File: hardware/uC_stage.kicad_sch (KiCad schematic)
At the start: 0 parts

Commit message: Updates to structure of the schematic. Minor funcitonality adjustments.
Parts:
- added C1, C2 (x4): 1u, Capacitor_SMD:C_0805_2012Metric_Pad1.18x1.45mm_HandSolder, symbol Device:C_Small
- added C2 (x4): 0.1u, Capacitor_SMD:C_0805_2012Metric_Pad1.18x1.45mm_HandSolder, symbol Device:C_Small
- added C2: 10u, Capacitor_SMD:C_0805_2012Metric_Pad1.18x1.45mm_HandSolder, symbol Device:C_Small
- added H1, H2, H3, H4: ~, MountingHole:MountingHole_3.2mm_M3_Pad_Via, symbol Mechanical:MountingHole_Pad
- added R41, R42: ?, Resistor_SMD:R_0805_2012Metric_Pad1.20x1.40mm_HandSolder, symbol Device:R_Small
- added R43, R44, R45: 10k, Resistor_SMD:R_0805_2012Metric_Pad1.20x1.40mm_HandSolder, symbol Device:R_Small
- added U10: STM32F042F6Px, Package_SO:TSSOP-20_4.4x6.5mm_P0.65mm, symbol MCU_ST_STM32F0:STM32F042F6Px
- added U2: MIC5504-1.2YM5, Package_TO_SOT_SMD:SOT-23-5_HandSoldering, symbol Regulator_Linear:MIC5504-1.2YM5
- added U8: MCP4728, Package_SO:MSOP-10_3x3mm_P0.5mm, symbol Analog_DAC:MCP4728
- added U9: DPO2036, User_USB_Protection:UQFN2020-12, symbol User_USB_Protection:DPO2036
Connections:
- new net: C2.1, U9.5 (CB)
- new net: R43.1, U8.6 (VOUTA)
- new net: R44.2, U8.7 (VOUTB)
- new net 3V3_SUPPLY_L: C2.1, C2.1, C2.1, C2.1, C2.1, C2.1, R41.1, R42.1, R45.1, U10.16 (VDD), U10.5 (VDDA), U2.5 (VOUT), U8.1 (VDD), U9.12 (VSYS)
- new net 5V0_SUPPLY_G: C1.1, U2.1 (VIN), U2.3 (EN)
- new net GND: C1.2, C2.2, C2.2, C2.2, C2.2, C2.2, C2.2, C2.2, C2.2, C2.2, H1.1, H2.1, H3.1, H4.1, U10.15 (VSSA), U2.2 (GND), U8.10 (VSS), U9.11 (GND)
- new net USB_C_CC1_G: U9.3 (CC1C)
- new net USB_C_CC2_G: U9.4 (CC2C)
- new net USB_C_DNEG_G: U9.1 (SBU1C)
- new net USB_C_DPOS_G: U9.2 (SBU2C)
- new net USB_C_ISOLATED_DNEG: U9.10 (SBUS1S)
- new net USB_C_ISOLATED_DPOS: U9.9 (SBUS2S)
- new net dacNLDAC_dig_l: U8.4 (~{LDAC})
- new net dacOutA_ang_g: C2.1, R43.2
- new net dacOutB_ang_g: C2.1, R44.1
- new net dacRDY_dig_l: U8.5 (RDY/~{BSY})
- new net ucSCL_com_l: R42.2, U8.2 (SCL)
- new net ucSDA_com_l: R41.2, U8.3 (SDA)
- new net usbCIsolatorFaultc_dig_l: R45.2, U9.6 (FAULTB)
- no-connect marks 0 -> 4
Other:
- note added: "TODO: Check the footprint and symbol pins!"

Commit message: Began initial routing. Schematic still not fully complete.
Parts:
- removed H1, H2, H3, H4: ~, MountingHole:MountingHole_3.2mm_M3_Pad_Via, symbol Mechanical:MountingHole_Pad
- added SW500: RotaryEncoder_Switch, Rotary_Encoder:RotaryEncoder_Alps_EC11E-Switch_Vertical_H20mm, symbol Device:RotaryEncoder_Switch
- renumbered R41 to R400, R42 to R401, R43 to R402, R44 to R403, R45 to R404, U8 to U401, U9 to U402, U10 to U403
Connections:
- net 3V3_SUPPLY_L: no longer C2.1, C2.1, C2.1, C2.1, C2.1, R400.1, R401.1, R404.1, U2.5 (VOUT), U401.1 (VDD), U403.16 (VDD), U403.5 (VDDA)
- net ucSCL_com_l renamed UCSCL_COM_G
- net ucSDA_com_l renamed UCSDA_COM_G
- new net 3V3_SUPPLY_G: C2.1, C2.1, C2.1, C2.1, C2.1, R400.1, R401.1, R404.1, U2.5 (VOUT), U401.1 (VDD), U403.16 (VDD), U403.5 (VDDA)

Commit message: Routing close to completion. Pending review.
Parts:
- removed R400, R401: ?, Resistor_SMD:R_0805_2012Metric_Pad1.20x1.40mm_HandSolder, symbol Device:R_Small
- added R508, R509: 0R, Resistor_SMD:R_0805_2012Metric_Pad1.20x1.40mm_HandSolder, symbol Device:R_Small
- added R510, R511: ?, Resistor_SMD:R_0805_2012Metric_Pad1.20x1.40mm_HandSolder, symbol Device:R_Small
- added TP500 (x9): ~, TestPoint:TestPoint_Pad_D1.0mm, symbol Connector:TestPoint
- added TP519: 3V3, TestPoint:TestPoint_Pad_D1.0mm, symbol Connector:TestPoint
- added TP520: SWDIO, TestPoint:TestPoint_Pad_D1.0mm, symbol Connector:TestPoint
- added TP521: SWDCLK, TestPoint:TestPoint_Pad_D1.0mm, symbol Connector:TestPoint
- added TP522: GND, TestPoint:TestPoint_Pad_D1.0mm, symbol Connector:TestPoint
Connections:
- net 3V3_SUPPLY_L is gone; now on net 3V3_SUPPLY_G: C2.1, U402.12 (VSYS)
- net 3V3_SUPPLY_G: now also R510.1, R511.1, TP500.1, TP519.1
- net GND: now also SW500.C, SW500.S2, TP522.1
- net UCSCL_COM_G: now also U403.1 (PB8), R510.2
- net UCSDA_COM_G: now also U403.2 (PF0), R511.2
- net USB_C_DNEG_G: now also R508.1
- net USB_C_DPOS_G: now also R509.2
- net USB_C_ISOLATED_DNEG: now also U403.17 (PA9/PA11), R508.2
- net USB_C_ISOLATED_DPOS: now also U403.18 (PA10/PA12), R509.1
- net dacNLDAC_dig_l: now also U403.10 (PA4), TP500.1
- net dacOutA_ang_g: now also TP500.1
- net dacOutB_ang_g: now also TP500.1
- net dacRDY_dig_l: now also U403.9 (PA3), TP500.1
- net usbCIsolatorFaultc_dig_l: now also TP500.1
- net encoderA_dig_l: now reaches SW500.A
- net encoderA_dig_l: now also U403.6 (PA0), TP500.1
- net encoderB_dig_l: now reaches SW500.B
- net encoderB_dig_l: now also U403.7 (PA1), TP500.1
- net encoderSW_dig_l: now reaches SW500.S1
- net encoderSW_dig_l: now also U403.8 (PA2), TP500.1
- net opStage2A_ang_g: now reaches U403.11 (PA5)
- net opStage2B_ang_g: now reaches U403.12 (PA6)
- net swdio_com_l: now reaches U403.19 (PA13)
- net swdio_com_l: now also TP520.1
- net swdclk_com_l: now reaches U403.20 (PA14)
- net swdclk_com_l: now also TP521.1
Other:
- moved on the sheet: SW500

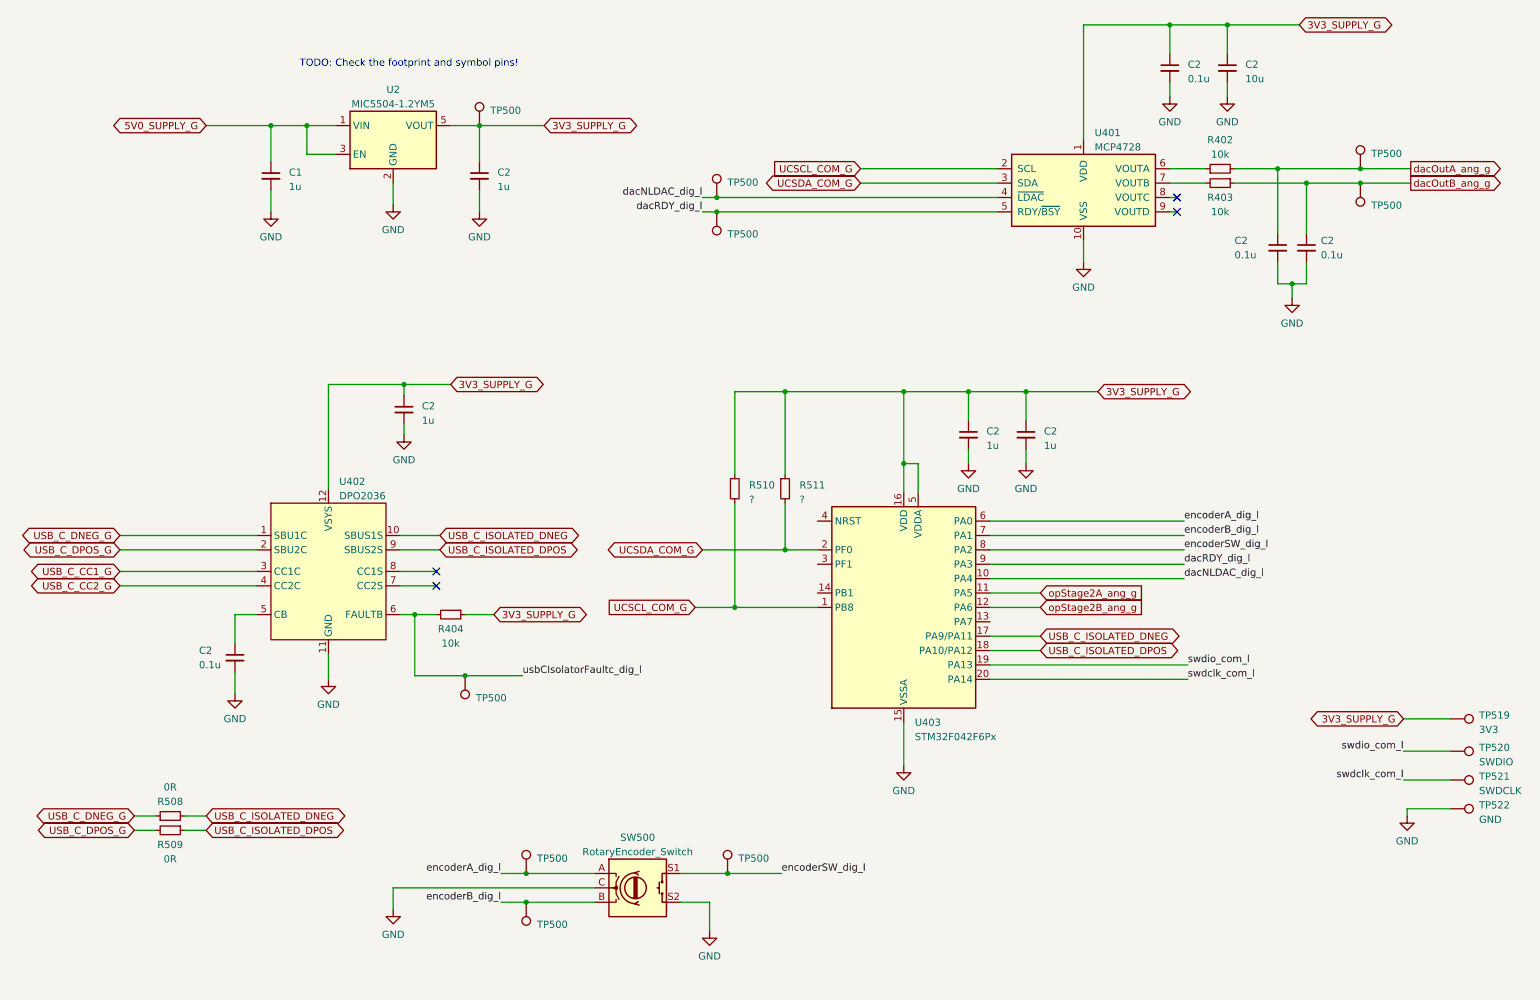
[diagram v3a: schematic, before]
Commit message: Added some doucmentation to MCP driver
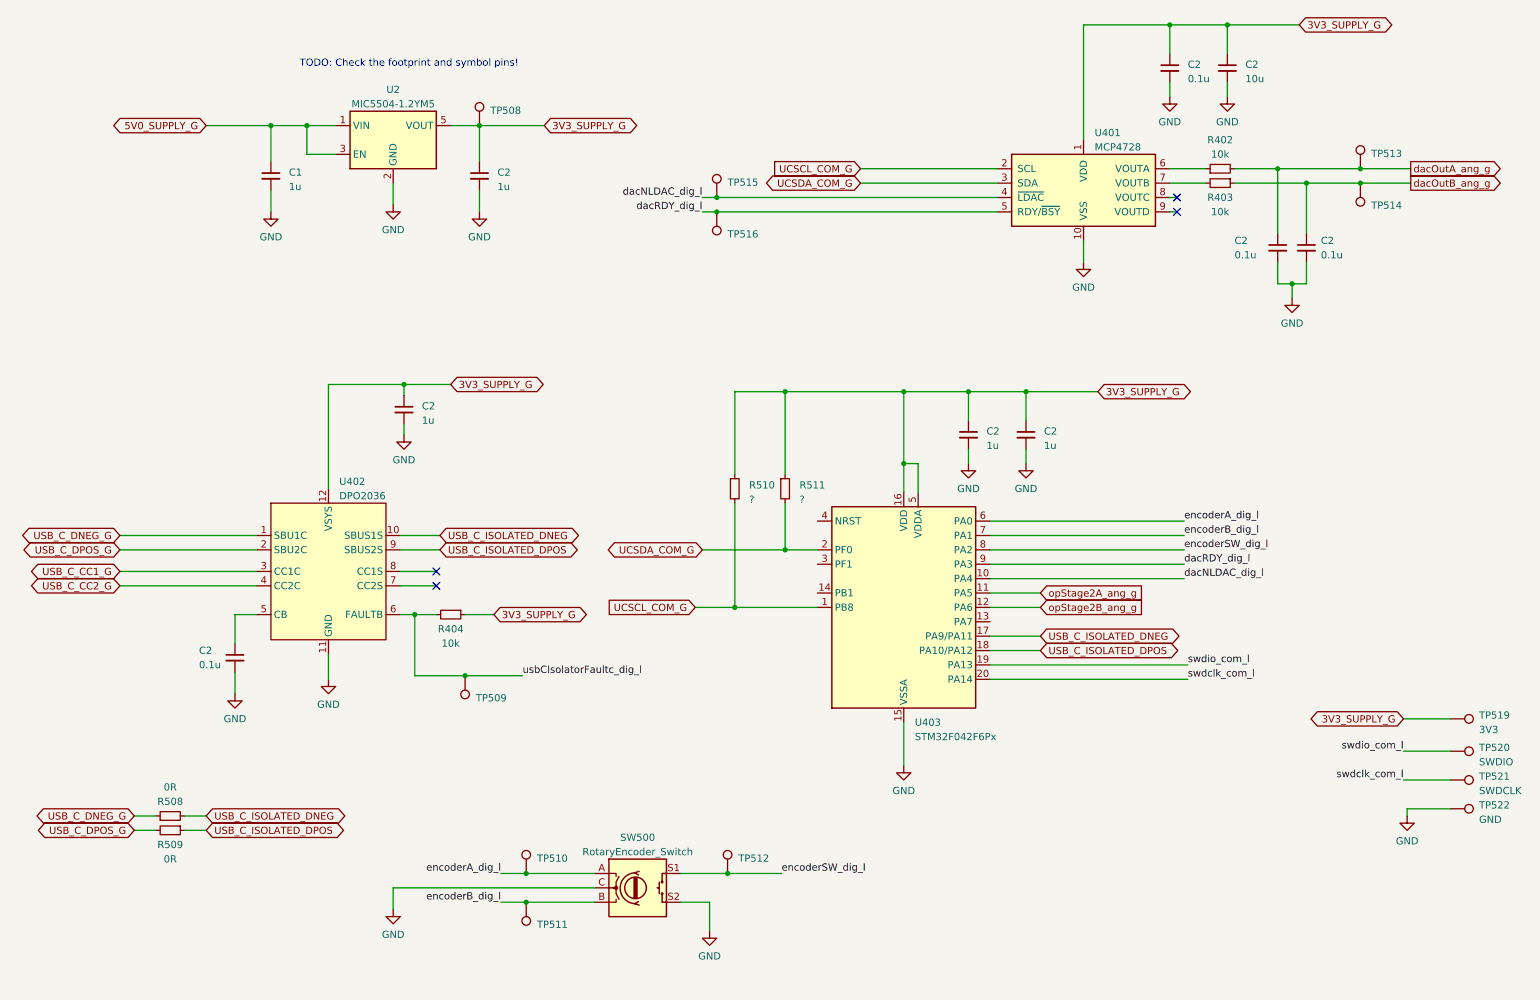
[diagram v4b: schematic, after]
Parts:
- renumbered TP500 to TP508, TP500 to TP509, TP500 to TP510, TP500 to TP511, TP500 to TP512, TP500 to TP513, TP500 to TP514, TP500 to TP515, TP500 to TP516
